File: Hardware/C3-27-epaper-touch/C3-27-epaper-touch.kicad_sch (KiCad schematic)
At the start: 61 parts, among them J1 AFC24-S24FIC-00, J2 USB_C_Programming, J3 Conn_01x06, J4 Conn_01x06_Female, J5 Groove sensor, Q1 Si1308, Q2 BC817, Q3 BC817, U1 ESP32-C3-WROOM-02-N4, U2 CP2102N-A02-GQFN28R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

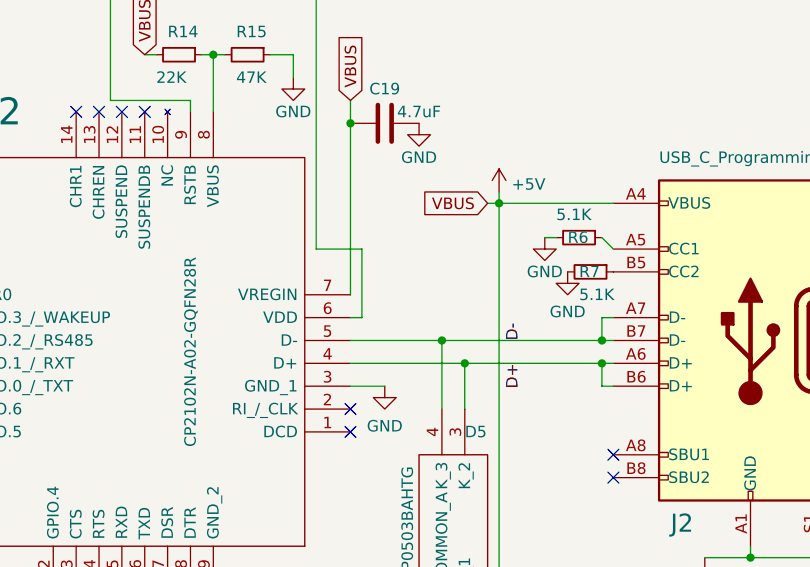
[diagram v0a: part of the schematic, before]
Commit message: Revert "C3 1.1 remove C13 does not seem to be necessary (near CP2102)"
This reverts commit e9bbdf2bfd8dbd0aba68dd1d7c9680fb7645ba6f.
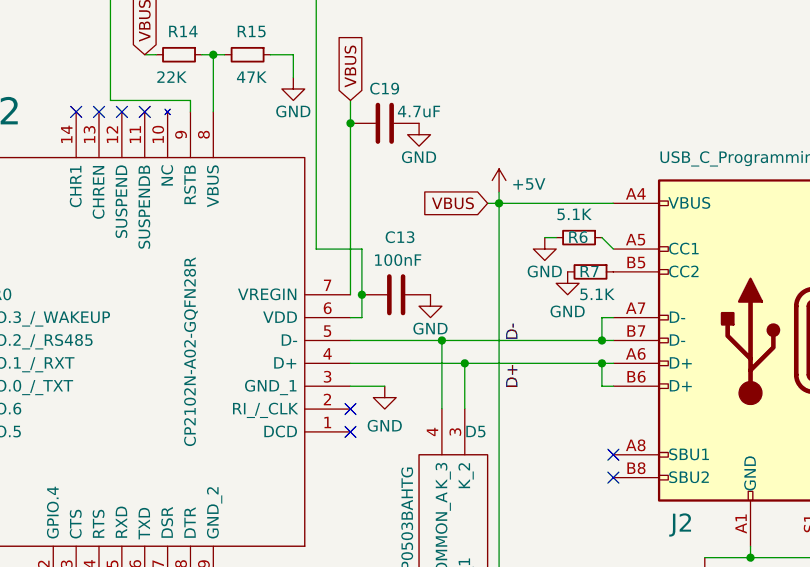
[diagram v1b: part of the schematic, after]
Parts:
- added C13: 100nF, Capacitor_SMD:C_0805_2012Metric, symbol Device:C
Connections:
- net GND: now also C13.2
- net at R13.1, U2.6 (VDD): now also C13.1
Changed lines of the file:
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@@
   (junction (at 99.06 74.93) (diameter 0) (color 0 0 0 0)
   )
+  (junction (at 326.39 68.58) (diameter 0) (color 0 0 0 0)
+  )
   (junction (at 68.58 72.39) (diameter 0) (color 0 0 0 0)
   )
@@
     (stroke (width 0) (type default) (color 0 0 0 0))
   )
-  (wire (pts (xy 326.39 63.5) (xy 326.39 71.12))
+  (wire (pts (xy 326.39 63.5) (xy 326.39 68.58))
     (stroke (width 0) (type default) (color 0 0 0 0))
   )
@@
     (stroke (width 0) (type default) (color 0 0 0 0))
   )
+  (wire (pts (xy 326.39 68.58) (xy 326.39 71.12))
+    (stroke (width 0) (type default) (color 0 0 0 0))
+  )
   (wire (pts (xy 66.04 110.49) (xy 66.04 106.68))
     (stroke (width 0) (type default) (color 0 0 0 0))
@@
     (pin "2")
   )
+  (symbol (lib_id "power:GND") (at 334.01 68.58 0) (unit 1)
+    (in_bom yes) (on_board yes)
+    (property "Reference" "#PWR020" (id 0) (at 334.01 74.93 0)
+      (effects (font (size 1.27 1.27)) hide)
+    )
+    (property "Value" "GND" (id 1) (at 334.01 72.39 0))
+    (property "Footprint" "" (id 2) (at 334.01 68.58 0)
+      (effects (font (size 1.27 1.27)) hide)
+    )
+    (property "Datasheet" "" (id 3) (at 334.01 68.58 0)
+      (effects (font (size 1.27 1.27)) hide)
+    )
+    (pin "1")
+  )
   (symbol (lib_id "Device:R_Small") (at 351.79 66.04 270) (unit 1)
     (in_bom yes) (on_board yes)
@@
     (pin "1")
   )
+  (symbol (lib_id "Device:C") (at 330.2 68.58 90) (unit 1)
+    (in_bom yes) (on_board yes)
+    (property "Reference" "C13" (id 0) (at 328.93 62.23 90)
+      (effects (font (size 1.27 1.27)) (justify right))
+    )
+    (property "Value" "100nF" (id 1) (at 327.66 64.77 90)
+      (effects (font (size 1.27 1.27)) (justify right))
+    )
+    (property "Footprint" "Capacitor_SMD:C_0805_2012Metric" (id 2) (at 334.01 67.6148 0)
+      (effects (font (size 1.27 1.27)) hide)
+    )
+    (property "Datasheet" "~" (id 3) (at 330.2 68.58 0)
+      (effects (font (size 1.27 1.27)) hide)
+    )
+    (property "LCSC" "C28233" (id 4) (at 330.2 68.58 0)
+      (effects (font (size 1.27 1.27)) hide)
+    )
+    (pin "1")
+    (pin "2")
+  )
   (symbol (lib_id "Device:C") (at 328.93 49.53 270) (unit 1)
     (in_bom yes) (on_board yes)
@@
       (reference "#PWR019") (unit 1) (value "GND") (footprint "")
     )
+    (path "/4a494997-8ec5-4aa3-918a-276b5f5c8d80"
+      (reference "#PWR020") (unit 1) (value "GND") (footprint "")
+    )
     (path "/9c88823a-1e84-4bce-8e32-cf963926ad4b"
       (reference "#PWR021") (unit 1) (value "+5V") (footprint "")
@@
       (reference "C12") (unit 1) (value "4.7uF") (footprint "Capacitor_SMD:C_0603_1608Metric")
     )
+    (path "/e010b6fb-2fb9-4bfd-b982-6a597128c5da"
+      (reference "C13") (unit 1) (value "100nF") (footprint "Capacitor_SMD:C_0805_2012Metric")
+    )
     (path "/858e1609-0117-4a64-a4cb-af2f22b2944b"

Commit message: C3 1.1 remove C13 does not seem to be necessary (near CP2102)
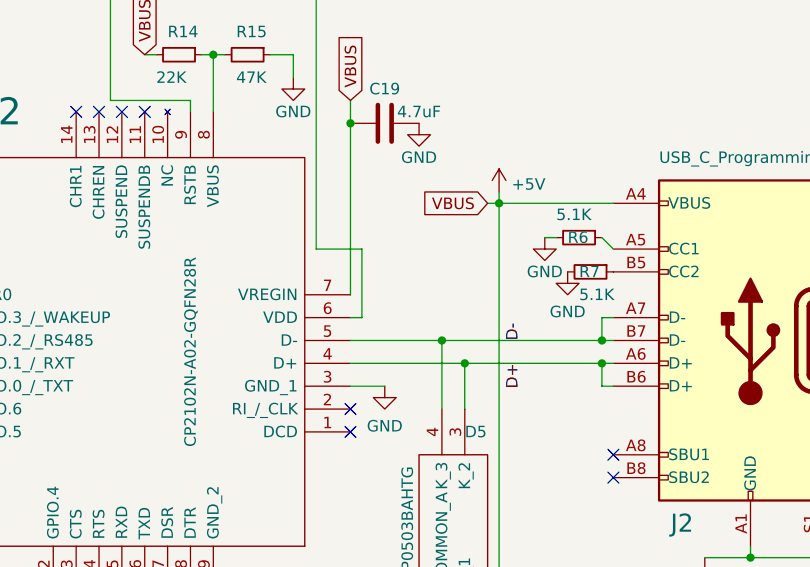
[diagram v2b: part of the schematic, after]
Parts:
- removed C13: 100nF, Capacitor_SMD:C_0805_2012Metric, symbol Device:C
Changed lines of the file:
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@@
   (junction (at 99.06 74.93) (diameter 0) (color 0 0 0 0)
   )
-  (junction (at 326.39 68.58) (diameter 0) (color 0 0 0 0)
-  )
   (junction (at 68.58 72.39) (diameter 0) (color 0 0 0 0)
   )
@@
     (stroke (width 0) (type default) (color 0 0 0 0))
   )
-  (wire (pts (xy 326.39 63.5) (xy 326.39 68.58))
+  (wire (pts (xy 326.39 63.5) (xy 326.39 71.12))
     (stroke (width 0) (type default) (color 0 0 0 0))
   )
@@
     (stroke (width 0) (type default) (color 0 0 0 0))
   )
-  (wire (pts (xy 326.39 68.58) (xy 326.39 71.12))
-    (stroke (width 0) (type default) (color 0 0 0 0))
-  )
   (wire (pts (xy 66.04 110.49) (xy 66.04 106.68))
     (stroke (width 0) (type default) (color 0 0 0 0))
@@
     (pin "2")
   )
-  (symbol (lib_id "power:GND") (at 334.01 68.58 0) (unit 1)
-    (in_bom yes) (on_board yes)
-    (property "Reference" "#PWR020" (id 0) (at 334.01 74.93 0)
-      (effects (font (size 1.27 1.27)) hide)
-    )
-    (property "Value" "GND" (id 1) (at 334.01 72.39 0))
-    (property "Footprint" "" (id 2) (at 334.01 68.58 0)
-      (effects (font (size 1.27 1.27)) hide)
-    )
-    (property "Datasheet" "" (id 3) (at 334.01 68.58 0)
-      (effects (font (size 1.27 1.27)) hide)
-    )
-    (pin "1")
-  )
   (symbol (lib_id "Device:R_Small") (at 351.79 66.04 270) (unit 1)
     (in_bom yes) (on_board yes)
@@
     (pin "1")
   )
-  (symbol (lib_id "Device:C") (at 330.2 68.58 90) (unit 1)
-    (in_bom yes) (on_board yes)
-    (property "Reference" "C13" (id 0) (at 328.93 62.23 90)
-      (effects (font (size 1.27 1.27)) (justify right))
-    )
-    (property "Value" "100nF" (id 1) (at 327.66 64.77 90)
-      (effects (font (size 1.27 1.27)) (justify right))
-    )
-    (property "Footprint" "Capacitor_SMD:C_0805_2012Metric" (id 2) (at 334.01 67.6148 0)
-      (effects (font (size 1.27 1.27)) hide)
-    )
-    (property "Datasheet" "~" (id 3) (at 330.2 68.58 0)
-      (effects (font (size 1.27 1.27)) hide)
-    )
-    (property "LCSC" "C28233" (id 4) (at 330.2 68.58 0)
-      (effects (font (size 1.27 1.27)) hide)
-    )
-    (pin "1")
-    (pin "2")
-  )
   (symbol (lib_id "Device:C") (at 328.93 49.53 270) (unit 1)
     (in_bom yes) (on_board yes)
@@
       (reference "#PWR019") (unit 1) (value "GND") (footprint "")
     )
-    (path "/4a494997-8ec5-4aa3-918a-276b5f5c8d80"
-      (reference "#PWR020") (unit 1) (value "GND") (footprint "")
-    )
     (path "/9c88823a-1e84-4bce-8e32-cf963926ad4b"
       (reference "#PWR021") (unit 1) (value "+5V") (footprint "")
@@
       (reference "C12") (unit 1) (value "4.7uF") (footprint "Capacitor_SMD:C_0603_1608Metric")
     )
-    (path "/e010b6fb-2fb9-4bfd-b982-6a597128c5da"
-      (reference "C13") (unit 1) (value "100nF") (footprint "Capacitor_SMD:C_0805_2012Metric")
-    )
     (path "/858e1609-0117-4a64-a4cb-af2f22b2944b"
